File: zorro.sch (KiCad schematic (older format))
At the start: 46 parts, among them U1 SN74LVC2T45, U10 SN74LVC8T245, U11 SN74LVC8T245, U12 SN74LVC8T245, U13 SN74LVC8T245, U14 SN74LVC8T245, U15 SN74LVC8T245, U16 SN74LVC2T45, U17 SN74LVC2T45, U18 SN74LVC2T45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

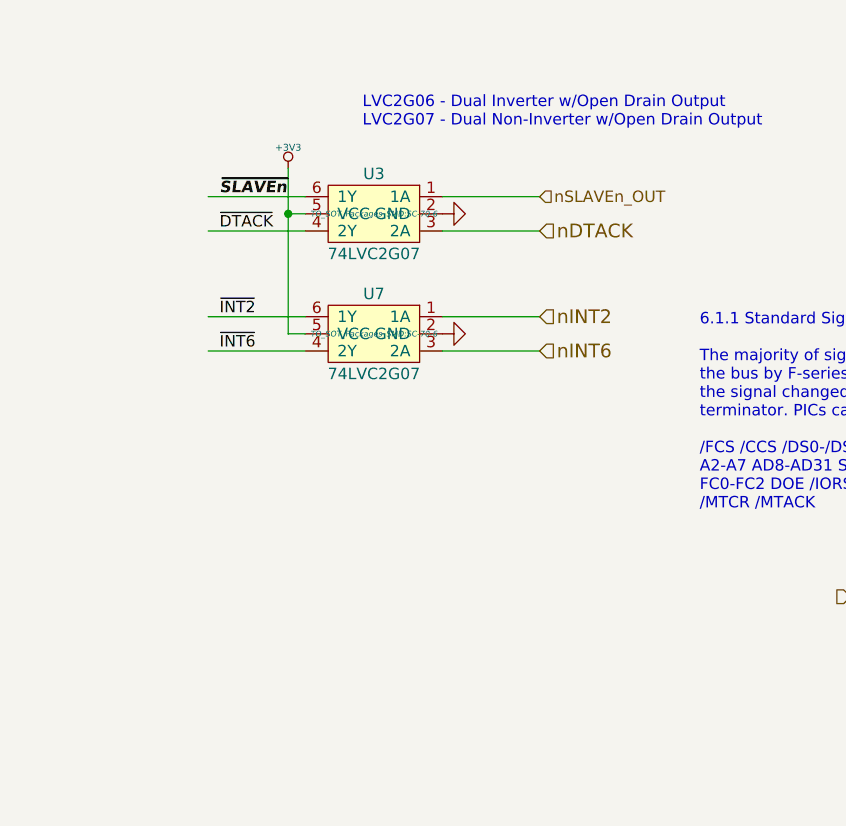
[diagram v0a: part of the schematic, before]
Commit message: Open drain signals
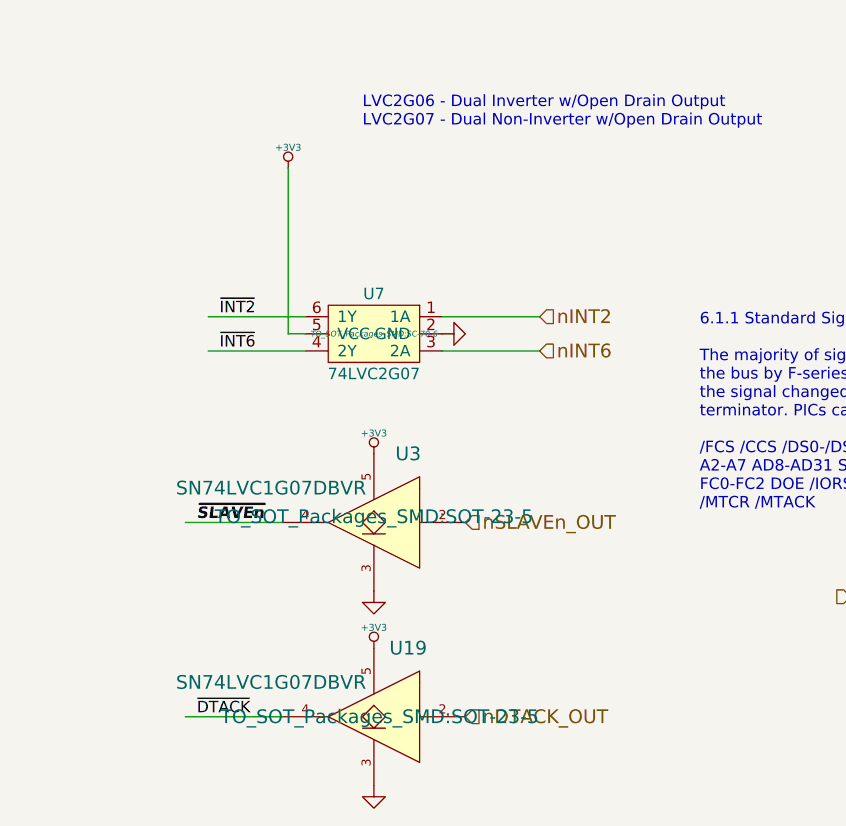
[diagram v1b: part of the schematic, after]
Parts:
- removed U3: 74LVC2G07, TO_SOT_Packages_SMD:SC-70-6, symbol 74LVC2G07
- added U19, U3: SN74LVC1G07DBVR, TO_SOT_Packages_SMD:SOT-23-5, symbol SN74LVC1G07DBVR
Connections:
- net labels added: nDTACK_OUT
- net labels removed: nDTACK
- wire segments 283 -> 280

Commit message: More routing
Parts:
- added U20: SN74LVC2T45, Housings_SSOP:TSSOP-8_3x3mm_Pitch0.65mm, symbol SN74LVC2T45
- U19, U3: value SN74LVC1G07DBVR -> SN74LVC1G07DCK; footprint TO_SOT_Packages_SMD:SOT-23-5 -> TO_SOT_Packages_SMD:SC-70-5
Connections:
- net labels added: nDTACK
- wire segments 280 -> 282

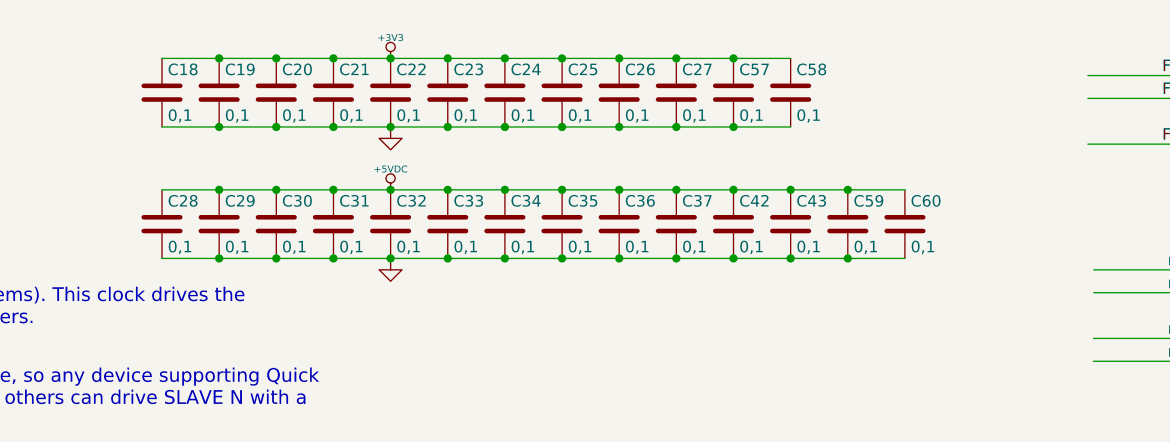
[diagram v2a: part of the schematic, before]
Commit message: More routing and caps
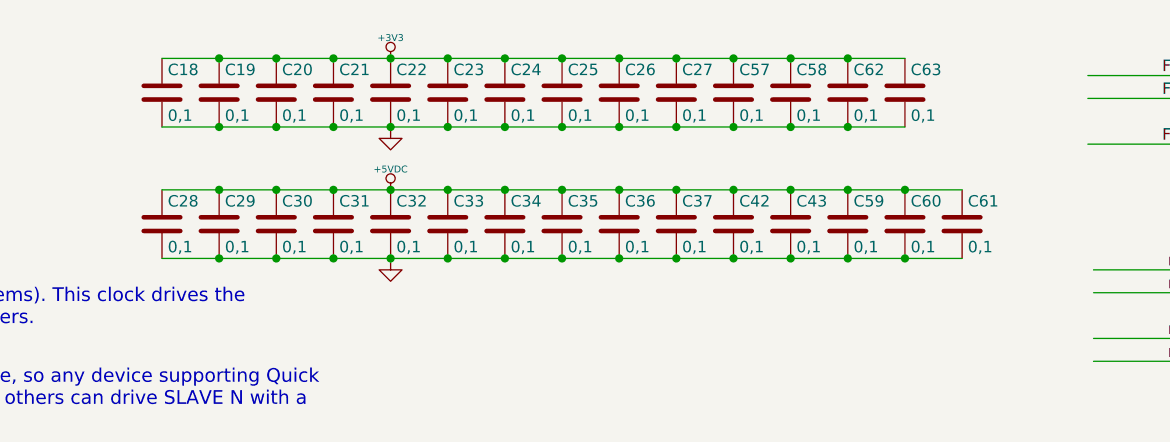
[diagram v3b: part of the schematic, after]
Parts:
- added C61, C62, C63: 0,1, Capacitors_SMD:C_0603, symbol C
